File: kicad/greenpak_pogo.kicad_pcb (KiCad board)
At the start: 2 copper layers, 7.6 x 14.4 mm, 4 parts

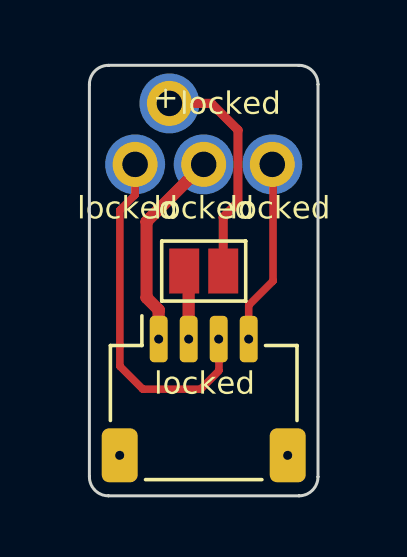
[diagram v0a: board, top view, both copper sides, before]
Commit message: Added to the pogo probe pullup resistors.
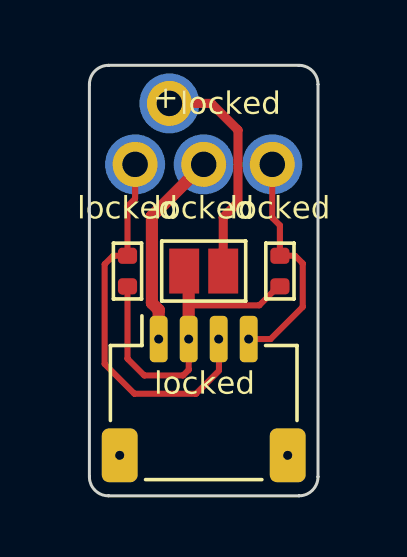
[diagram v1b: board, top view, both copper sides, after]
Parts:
- added REF**: R_0402_1005Metric, greenpak_pogo:R_0402_1005Metric, F.Cu at (2.54, 3.56)
- added REF**: R_0402_1005Metric, greenpak_pogo:R_0402_1005Metric, F.Cu at (-2.54, 3.56)
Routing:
- net (no net): track 34.1 -> 46.1 mm
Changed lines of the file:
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@@
+    )
+  )
+  (footprint "greenpak_pogo:R_0402_1005Metric" (layer "F.Cu")
+    (at 2.54 3.556 90)
+    (descr "Resistor SMD 0402 (1005 Metric), square (rectangular) end terminal, IPC_7351 nominal, (Body size source: IPC-SM-782 page 72, https://www.pcb-3d.com/wordpress/wp-content/uploads/ipc-sm-782a_amendment_1_and_2.pdf), generated with kicad-footprint-generator")
+    (tags "resistor")
+    (attr smd)
+    (fp_text reference "REF**" (at 0 -1.17 90) (layer "F.SilkS") hide
+        (effects (font (size 1 1) (thickness 0.15)))
+    )
+    (fp_text value "R_0402_1005Metric" (at 0 1.17 90) (layer "F.Fab") hide
+        (effects (font (size 1 1) (thickness 0.15)))
+    )
+    (fp_line (start -0.93 -0.47) (end 0.93 -0.47)
+      (stroke (width 0.12) (type solid)) (layer "F.SilkS"))
+    (fp_line (start -0.93 0.47) (end -0.93 -0.47)
+      (stroke (width 0.12) (type solid)) (layer "F.SilkS"))
+    (fp_line (start 0.93 -0.47) (end 0.93 0.47)
+      (stroke (width 0.12) (type solid)) (layer "F.SilkS"))
+    (fp_line (start 0.93 0.47) (end -0.93 0.47)
+      (stroke (width 0.12) (type solid)) (layer "F.SilkS"))
+    (fp_line (start -0.525 -0.27) (end 0.525 -0.27)
+      (stroke (width 0.1) (type solid)) (layer "F.Fab"))
+    (fp_line (start -0.525 0.27) (end -0.525 -0.27)
+      (stroke (width 0.1) (type solid)) (layer "F.Fab"))
+    (fp_line (start 0.525 -0.27) (end 0.525 0.27)
+      (stroke (width 0.1) (type solid)) (layer "F.Fab"))
+    (fp_line (start 0.525 0.27) (end -0.525 0.27)
+      (stroke (width 0.1) (type solid)) (layer "F.Fab"))
+    (pad "1" smd roundrect (at -0.51 0 90) (size 0.54 0.64) (layers "F.Cu" "F.Paste" "F.Mask") (roundrect_rratio 0.25))
+    (pad "2" smd roundrect (at 0.51 0 90) (size 0.54 0.64) (layers "F.Cu" "F.Paste" "F.Mask") (roundrect_rratio 0.25))
+    (model "${KICAD6_3DMODEL_DIR}/Resistor_SMD.3dshapes/R_0402_1005Metric.wrl"
+      (offset (xyz 0 0 0))
+      (scale (xyz 1 1 1))
+      (rotate (xyz 0 0 0))
     )
   )
@@
     (pad "1" smd rect (at -0.65 0) (size 1 1.5) (layers "F.Cu" "F.Mask"))
     (pad "2" smd rect (at 0.65 0) (size 1 1.5) (layers "F.Cu" "F.Mask"))
+  )
+  (footprint "greenpak_pogo:R_0402_1005Metric" (layer "F.Cu")
+    (at -2.54 3.556 90)
+    (descr "Resistor SMD 0402 (1005 Metric), square (rectangular) end terminal, IPC_7351 nominal, (Body size source: IPC-SM-782 page 72, https://www.pcb-3d.com/wordpress/wp-content/uploads/ipc-sm-782a_amendment_1_and_2.pdf), generated with kicad-footprint-generator")
+    (tags "resistor")
+    (attr smd)
+    (fp_text reference "REF**" (at 0 -1.17 90) (layer "F.SilkS") hide
+        (effects (font (size 1 1) (thickness 0.15)))
+    )
+    (fp_text value "R_0402_1005Metric" (at 0 1.17 90) (layer "F.Fab") hide
+        (effects (font (size 1 1) (thickness 0.15)))
+    )
+    (fp_line (start -0.93 -0.47) (end 0.93 -0.47)
+      (stroke (width 0.12) (type solid)) (layer "F.SilkS"))
+    (fp_line (start -0.93 0.47) (end -0.93 -0.47)
+      (stroke (width 0.12) (type solid)) (layer "F.SilkS"))
+    (fp_line (start 0.93 -0.47) (end 0.93 0.47)
+      (stroke (width 0.12) (type solid)) (layer "F.SilkS"))
+    (fp_line (start 0.93 0.47) (end -0.93 0.47)
+      (stroke (width 0.12) (type solid)) (layer "F.SilkS"))
+    (fp_line (start -0.525 -0.27) (end 0.525 -0.27)
+      (stroke (width 0.1) (type solid)) (layer "F.Fab"))
+    (fp_line (start -0.525 0.27) (end -0.525 -0.27)
+      (stroke (width 0.1) (type solid)) (layer "F.Fab"))
+    (fp_line (start 0.525 -0.27) (end 0.525 0.27)
+      (stroke (width 0.1) (type solid)) (layer "F.Fab"))
+    (fp_line (start 0.525 0.27) (end -0.525 0.27)
+      (stroke (width 0.1) (type solid)) (layer "F.Fab"))
+    (pad "1" smd roundrect (at -0.51 0 90) (size 0.54 0.64) (layers "F.Cu" "F.Paste" "F.Mask") (roundrect_rratio 0.25))
+    (pad "2" smd roundrect (at 0.51 0 90) (size 0.54 0.64) (layers "F.Cu" "F.Paste" "F.Mask") (roundrect_rratio 0.25))
+    (model "${KICAD6_3DMODEL_DIR}/Resistor_SMD.3dshapes/R_0402_1005Metric.wrl"
+      (offset (xyz 0 0 0))
+      (scale (xyz 1 1 1))
+      (rotate (xyz 0 0 0))
+    )
   )
   (footprint "greenpak_pogo:QWIIC_logo_6mm" (layer "B.Cu")
@@
     (effects (font (size 0.7 0.7) (thickness 0.1)) (justify left bottom))
   )
+  (segment (start 2.4872 4.066) (end 2.54 4.066) (width 0.2032) (layer "F.Cu") (net 0))
   (segment (start 1.143 -1.143) (end 0.254 -2.032) (width 0.3048) (layer "F.Cu") (net 0))
-  (segment (start -1.905 1.905) (end 0 0) (width 0.4064) (layer "F.Cu") (net 0))
+  (segment (start 3.046 3.046) (end 2.54 3.046) (width 0.2032) (layer "F.Cu") (net 0))
+  (segment (start 1.8542 4.699) (end 2.4872 4.066) (width 0.2032) (layer "F.Cu") (net 0))
+  (segment (start 2.2286 5.8232) (end 3.302 4.7498) (width 0.2032) (layer "F.Cu") (net 0))
+  (segment (start -3.302 6.6548) (end -2.3114 7.6454) (width 0.2032) (layer "F.Cu") (net 0))
+  (segment (start -2.54 3.046) (end -3.0206 3.046) (width 0.2032) (layer "F.Cu") (net 0))
+  (segment (start -0.5 6.85) (end -0.6858 7.0358) (width 0.2032) (layer "F.Cu") (net 0))
   (segment (start -0.65 3.175) (end -0.5 3.325) (width 0.4064) (layer "F.Cu") (net 0))
+  (segment (start -1.7272 1.7272) (end 0 0) (width 0.4064) (layer "F.Cu") (net 0))
+  (segment (start -3.0206 3.046) (end -3.302 3.3274) (width 0.2032) (layer "F.Cu") (net 0))
+  (segment (start -0.5 4.699) (end 1.8542 4.699) (width 0.2032) (layer "F.Cu") (net 0))
+  (segment (start -2.6924 4.2184) (end -2.54 4.066) (width 0.254) (layer "F.Cu") (net 0))
+  (segment (start -0.254 7.6454) (end 0.508 6.8834) (width 0.2032) (layer "F.Cu") (net 0))
+  (segment (start -2.54 1.397) (end -2.54 3.046) (width 0.2032) (layer "F.Cu") (net 0))
   (segment (start -0.5 3.325) (end -0.5 5.62) (width 0.4064) (layer "F.Cu") (net 0))
-  (segment (start 1.5 5.62) (end 1.5 4.6976) (width 0.254) (layer "F.Cu") (net 0))
-  (segment (start 0.508 5.8312) (end 0.508 6.858) (width 0.254) (layer "F.Cu") (net 0))
+  (segment (start -1.9812 7.0358) (end -2.54 6.477) (width 0.2032) (layer "F.Cu") (net 0))
+  (segment (start -2.3114 7.6454) (end -0.254 7.6454) (width 0.2032) (layer "F.Cu") (net 0))
+  (segment (start -2.54 6.477) (end -2.54 4.066) (width 0.2032) (layer "F.Cu") (net 0))
+  (segment (start 0.508 5.8312) (end 0.508 6.858) (width 0.2032) (layer "F.Cu") (net 0))
   (segment (start 2.3114 0.0254) (end 2.286 0) (width 0.254) (layer "F.Cu") (net 0))
-  (segment (start 0.508 6.8834) (end -0.1016 7.493) (width 0.254) (layer "F.Cu") (net 0))
-  (segment (start -2.794 1.524) (end -2.286 1.016) (width 0.254) (layer "F.Cu") (net 0))
-  (segment (start -2.032 7.493) (end -2.794 6.731) (width 0.254) (layer "F.Cu") (net 0))
+  (segment (start 1.5 5.8232) (end 2.2286 5.8232) (width 0.2032) (layer "F.Cu") (net 0))
+  (segment (start -3.302 3.3274) (end -3.302 6.6548) (width 0.2032) (layer "F.Cu") (net 0))
+  (segment (start 3.302 4.7498) (end 3.302 3.302) (width 0.2032) (layer "F.Cu") (net 0))
   (segment (start 0.65 3.175) (end 0.65 1.763) (width 0.3048) (layer "F.Cu") (net 0))
-  (segment (start -1.5 4.85) (end -1.905 4.445) (width 0.4064) (layer "F.Cu") (net 0))
-  (segment (start -2.286 1.016) (end -2.286 0) (width 0.254) (layer "F.Cu") (net 0))
+  (segment (start -0.6858 7.0358) (end -1.9812 7.0358) (width 0.2032) (layer "F.Cu") (net 0))
+  (segment (start -1.7272 4.6228) (end -1.7272 1.7272) (width 0.4064) (layer "F.Cu") (net 0))
+  (segment (start -1.5 4.85) (end -1.7272 4.6228) (width 0.4064) (layer "F.Cu") (net 0))
+  (segment (start -2.54 3.046) (end -2.5146 3.0206) (width 0.254) (layer "F.Cu") (net 0))
   (segment (start 0.65 1.763) (end 1.143 1.27) (width 0.3048) (layer "F.Cu") (net 0))
-  (segment (start -0.1016 7.493) (end -2.032 7.493) (width 0.254) (layer "F.Cu") (net 0))
-  (segment (start -1.905 4.445) (end -1.905 1.905) (width 0.4064) (layer "F.Cu") (net 0))
-  (segment (start 1.5 4.6976) (end 2.3114 3.8862) (width 0.254) (layer "F.Cu") (net 0))
-  (segment (start 2.3114 3.8862) (end 2.3114 0.0254) (width 0.254) (layer "F.Cu") (net 0))
+  (segment (start -0.5 5.8232) (end -0.5 6.85) (width 0.2032) (layer "F.Cu") (net 0))
   (segment (start 1.143 1.27) (end 1.143 -1.143) (width 0.3048) (layer "F.Cu") (net 0))
+  (segment (start 2.286 1.778) (end 2.54 2.032) (width 0.2032) (layer "F.Cu") (net 0))
+  (segment (start -2.286 1.143) (end -2.54 1.397) (width 0.2032) (layer "F.Cu") (net 0))
+  (segment (start -2.286 0) (end -2.286 1.143) (width 0.2032) (layer "F.Cu") (net 0))
   (segment (start -1.5 5.62) (end -1.5 4.85) (width 0.4064) (layer "F.Cu") (net 0))
+  (segment (start 2.286 0) (end 2.286 1.778) (width 0.2032) (layer "F.Cu") (net 0))
+  (segment (start 2.54 2.032) (end 2.54 3.046) (width 0.2032) (layer "F.Cu") (net 0))
   (segment (start 0.254 -2.032) (end -1.143 -2.032) (width 0.3048) (layer "F.Cu") (net 0))
-  (segment (start -2.794 6.731) (end -2.794 1.524) (width 0.254) (layer "F.Cu") (net 0))
+  (segment (start 3.302 3.302) (end 3.046 3.046) (width 0.2032) (layer "F.Cu") (net 0))
   (group "" locked (id 2972b439-deb4-4103-8004-66da0f130234)
     (members

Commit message: Updated pogo socket to new dimensions.
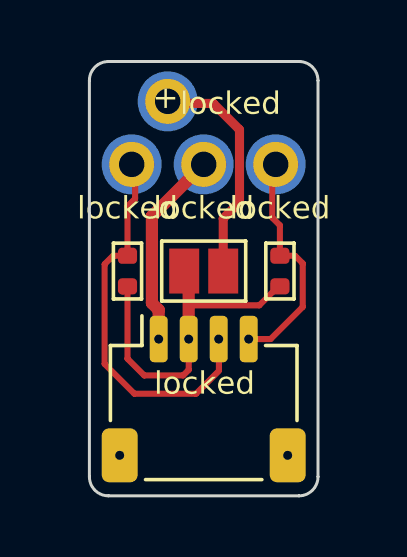
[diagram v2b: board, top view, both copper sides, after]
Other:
- board size 7.6 x 14.4 mm -> 7.6 x 14.5 mm
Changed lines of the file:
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@@
         (effects (font (size 1 1) (thickness 0.15)))
     )
-    (fp_circle (center -2.286 0) (end -1.436 0)
+    (fp_circle (center -2.4 0) (end -1.55 0)
       (stroke (width 0.3) (type solid)) (fill none) (layer "B.Cu"))
-    (fp_circle (center -1.143 -2.032) (end -0.293 -2.032)
+    (fp_circle (center -1.2 -2.1) (end -0.35 -2.1)
       (stroke (width 0.3) (type solid)) (fill none) (layer "B.Cu"))
     (fp_circle (center 0 0) (end 0.85 0)
       (stroke (width 0.3) (type solid)) (fill none) (layer "B.Cu"))
-    (fp_circle (center 2.286 0) (end 3.136 0)
+    (fp_circle (center 2.4 0) (end 3.25 0)
       (stroke (width 0.3) (type solid)) (fill none) (layer "B.Cu"))
-    (fp_circle (center -2.286 0) (end -1.436 0)
+    (fp_circle (center -2.4 0) (end -1.55 0)
       (stroke (width 0.3) (type solid)) (fill none) (layer "B.Mask"))
-    (fp_circle (center -1.143 -2.032) (end -0.293 -2.032)
+    (fp_circle (center -1.2 -2.1) (end -0.35 -2.1)
       (stroke (width 0.3) (type solid)) (fill none) (layer "B.Mask"))
     (fp_circle (center 0 0) (end 0.85 0)
       (stroke (width 0.3) (type solid)) (fill none) (layer "B.Mask"))
-    (fp_circle (center 2.286 0) (end 3.136 0)
+    (fp_circle (center 2.4 0) (end 3.25 0)
       (stroke (width 0.3) (type solid)) (fill none) (layer "B.Mask"))
-    (pad "1" thru_hole circle locked (at -2.286 0) (size 1.5 1.5) (drill 0.85) (layers "*.Cu" "*.Mask"))
+    (pad "1" thru_hole circle locked (at -2.4 0) (size 1.5 1.5) (drill 0.85) (layers "*.Cu" "*.Mask"))
     (pad "2" thru_hole circle locked (at 0 0) (size 1.5 1.5) (drill 0.85) (layers "*.Cu" "*.Mask"))
-    (pad "3" thru_hole circle locked (at 2.286 0) (size 1.5 1.5) (drill 0.85) (layers "*.Cu" "*.Mask"))
-    (pad "4" thru_hole circle locked (at -1.143 -2.032) (size 1.5 1.5) (drill 0.85) (layers "*.Cu" "*.Mask"))
+    (pad "3" thru_hole circle locked (at 2.4 0) (size 1.5 1.5) (drill 0.85) (layers "*.Cu" "*.Mask"))
+    (pad "4" thru_hole circle locked (at -1.2 -2.1) (size 1.5 1.5) (drill 0.85) (layers "*.Cu" "*.Mask"))
     (model "${KIPRJMOD}/3d_models/POGO_PINS.step"
       (offset (xyz 0 0 -1.6))
@@
   (gr_line (start 3.175 11.049) (end -3.175 11.049)
     (stroke (width 0.1) (type default)) (layer "Edge.Cuts"))
-  (gr_arc (start 3.175 -3.302) (mid 3.624013 -3.116013) (end 3.81 -2.667)
+  (gr_arc (start 3.175 -3.429) (mid 3.624013 -3.243013) (end 3.81 -2.794)
     (stroke (width 0.1) (type default)) (layer "Edge.Cuts"))
-  (gr_line (start -3.81 10.414) (end -3.81 -2.667)
+  (gr_line (start -3.81 10.414) (end -3.81 -2.794)
     (stroke (width 0.1) (type default)) (layer "Edge.Cuts"))
   (gr_arc (start -3.175 11.049) (mid -3.624013 10.863013) (end -3.81 10.414)
     (stroke (width 0.1) (type default)) (layer "Edge.Cuts"))
-  (gr_line (start -3.175 -3.302) (end 3.175 -3.302)
+  (gr_line (start -3.175 -3.429) (end 3.175 -3.429)
     (stroke (width 0.1) (type default)) (layer "Edge.Cuts"))
-  (gr_arc (start -3.81 -2.667) (mid -3.624013 -3.116013) (end -3.175 -3.302)
+  (gr_arc (start -3.81 -2.794) (mid -3.624013 -3.243013) (end -3.175 -3.429)
     (stroke (width 0.1) (type default)) (layer "Edge.Cuts"))
-  (gr_line (start 3.81 -2.667) (end 3.81 10.414)
+  (gr_line (start 3.81 -2.794) (end 3.81 10.414)
     (stroke (width 0.1) (type default)) (layer "Edge.Cuts"))
   (gr_text locked "VCC" (at -0.508 10.7188 90) (layer "B.SilkS")
@@
   )
   (segment (start 2.4872 4.066) (end 2.54 4.066) (width 0.2032) (layer "F.Cu") (net 0))
-  (segment (start 1.143 -1.143) (end 0.254 -2.032) (width 0.3048) (layer "F.Cu") (net 0))
   (segment (start 3.046 3.046) (end 2.54 3.046) (width 0.2032) (layer "F.Cu") (net 0))
   (segment (start 1.8542 4.699) (end 2.4872 4.066) (width 0.2032) (layer "F.Cu") (net 0))
@@
   (segment (start -0.5 4.699) (end 1.8542 4.699) (width 0.2032) (layer "F.Cu") (net 0))
   (segment (start -2.6924 4.2184) (end -2.54 4.066) (width 0.254) (layer "F.Cu") (net 0))
+  (segment (start 0.65 3.175) (end 0.65 1.8011) (width 0.3048) (layer "F.Cu") (net 0))
   (segment (start -0.254 7.6454) (end 0.508 6.8834) (width 0.2032) (layer "F.Cu") (net 0))
   (segment (start -2.54 1.397) (end -2.54 3.046) (width 0.2032) (layer "F.Cu") (net 0))
@@
   (segment (start 0.508 5.8312) (end 0.508 6.858) (width 0.2032) (layer "F.Cu") (net 0))
   (segment (start 2.3114 0.0254) (end 2.286 0) (width 0.254) (layer "F.Cu") (net 0))
+  (segment (start 0.65 1.8011) (end 1.1938 1.2573) (width 0.3048) (layer "F.Cu") (net 0))
   (segment (start 1.5 5.8232) (end 2.2286 5.8232) (width 0.2032) (layer "F.Cu") (net 0))
   (segment (start -3.302 3.3274) (end -3.302 6.6548) (width 0.2032) (layer "F.Cu") (net 0))
   (segment (start 3.302 4.7498) (end 3.302 3.302) (width 0.2032) (layer "F.Cu") (net 0))
-  (segment (start 0.65 3.175) (end 0.65 1.763) (width 0.3048) (layer "F.Cu") (net 0))
+  (segment (start 1.1938 -1.1557) (end 0.3175 -2.032) (width 0.3048) (layer "F.Cu") (net 0))
   (segment (start -0.6858 7.0358) (end -1.9812 7.0358) (width 0.2032) (layer "F.Cu") (net 0))
   (segment (start -1.7272 4.6228) (end -1.7272 1.7272) (width 0.4064) (layer "F.Cu") (net 0))
   (segment (start -1.5 4.85) (end -1.7272 4.6228) (width 0.4064) (layer "F.Cu") (net 0))
   (segment (start -2.54 3.046) (end -2.5146 3.0206) (width 0.254) (layer "F.Cu") (net 0))
-  (segment (start 0.65 1.763) (end 1.143 1.27) (width 0.3048) (layer "F.Cu") (net 0))
+  (segment (start 0.3175 -2.032) (end -1.143 -2.032) (width 0.3048) (layer "F.Cu") (net 0))
   (segment (start -0.5 5.8232) (end -0.5 6.85) (width 0.2032) (layer "F.Cu") (net 0))
-  (segment (start 1.143 1.27) (end 1.143 -1.143) (width 0.3048) (layer "F.Cu") (net 0))
+  (segment (start 1.1938 1.2573) (end 1.1938 -1.1557) (width 0.3048) (layer "F.Cu") (net 0))
   (segment (start 2.286 1.778) (end 2.54 2.032) (width 0.2032) (layer "F.Cu") (net 0))
   (segment (start -2.286 1.143) (end -2.54 1.397) (width 0.2032) (layer "F.Cu") (net 0))
@@
   (segment (start 2.286 0) (end 2.286 1.778) (width 0.2032) (layer "F.Cu") (net 0))
   (segment (start 2.54 2.032) (end 2.54 3.046) (width 0.2032) (layer "F.Cu") (net 0))
-  (segment (start 0.254 -2.032) (end -1.143 -2.032) (width 0.3048) (layer "F.Cu") (net 0))
   (segment (start 3.302 3.302) (end 3.046 3.046) (width 0.2032) (layer "F.Cu") (net 0))
   (group "" locked (id 2972b439-deb4-4103-8004-66da0f130234)

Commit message: Added schematic.
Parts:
- R1, R2: renamed from REF**; value R_0402_1005Metric -> 5K
- renumbered REF** to J1, REF** to J2, REF** to JP1
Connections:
- J1 pad 1: (no net) -> GNDD
- J1 pad 2: (no net) -> Net-(J1-Pin_2)
- J1 pad 3: (no net) -> /SDA
- J1 pad 4: (no net) -> /SCL
- J2 pad 1: (no net) -> /SDA
- J2 pad 2: (no net) -> GNDD
- J2 pad 3: (no net) -> /SCL
- J2 pad 4: (no net) -> VCC
- JP1 pad 1: (no net) -> Net-(J1-Pin_2)
- JP1 pad 2: (no net) -> VCC
- R1 pad 1: (no net) -> VCC
- R1 pad 2: (no net) -> /SDA
- R2 pad 1: (no net) -> VCC
- R2 pad 2: (no net) -> /SCL
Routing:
- net (no net): track 46.2 -> 0.00 mm
- net /SDA: track 0.00 -> 13.0 mm
- net /SCL: track 0.00 -> 7.75 mm
- net VCC: track 0.00 -> 7.47 mm
- net GNDD: track 0.00 -> 6.43 mm
- net Net-(J1-Pin_2): track 0.00 -> 2.51 mm
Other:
- board text removed: "+"
